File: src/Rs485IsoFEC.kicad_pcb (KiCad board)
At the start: 2 copper layers, 24 x 27.9 mm, 29 parts, among them J1 B3B-XH-A, P1 105444-0001, Q1 DMP3099L-13, U1 FT232RL, U2 ADM2682E

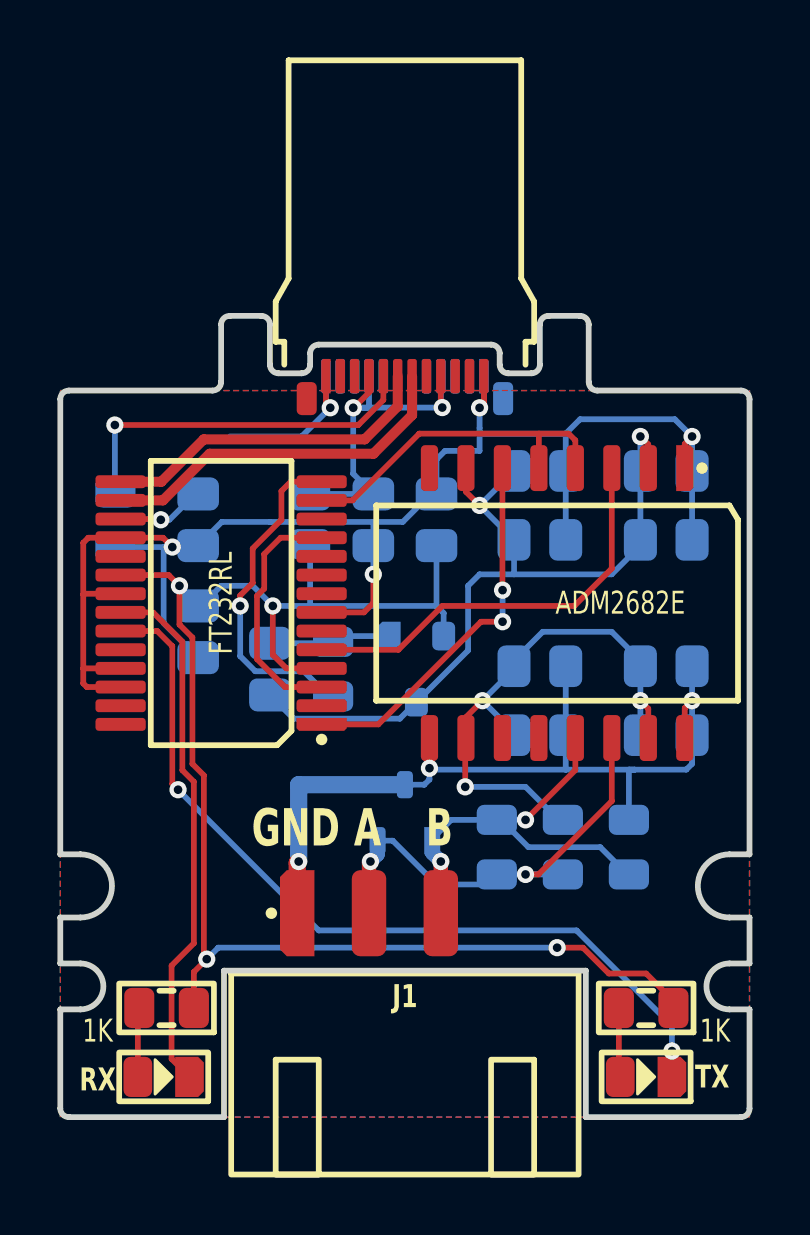
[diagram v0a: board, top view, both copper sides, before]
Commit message: Removed fail-safe termination
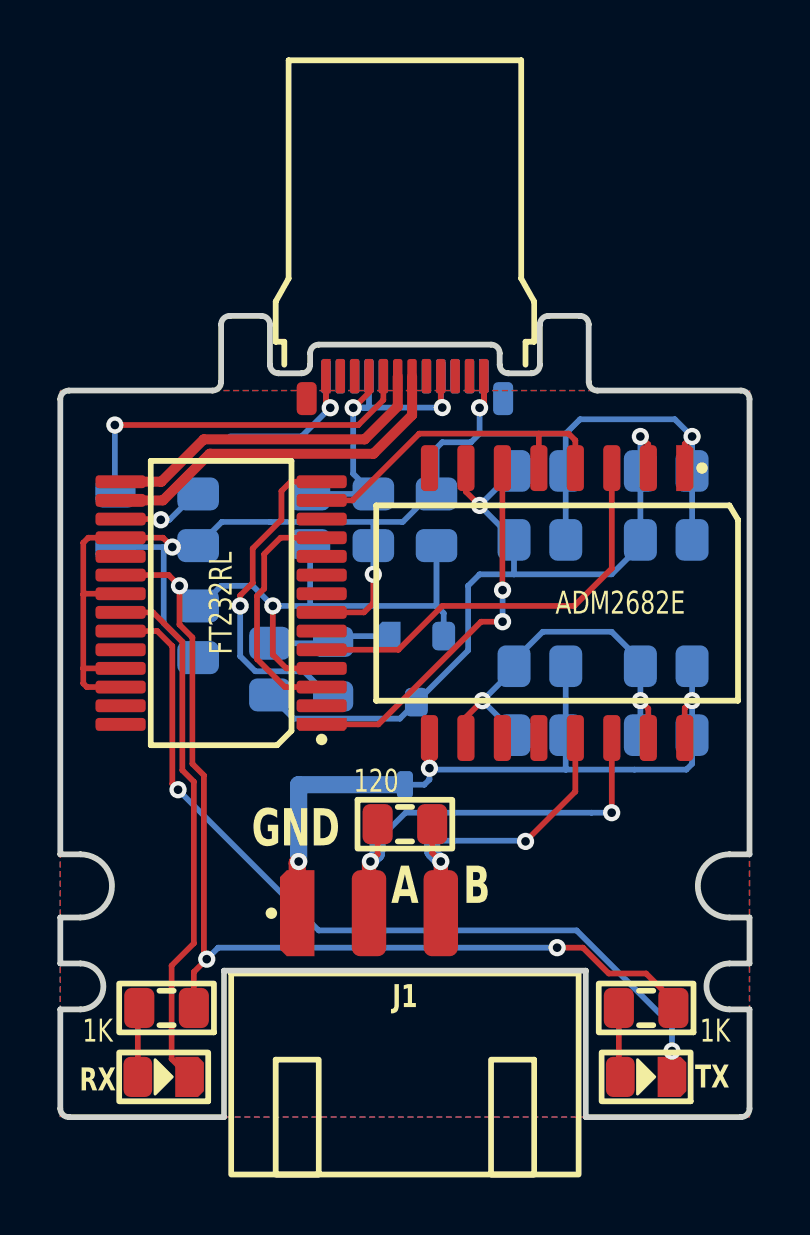
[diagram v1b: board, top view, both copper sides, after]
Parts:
- removed the R2 at (37.5, 38.5)
- removed the R3 at (39.8, 38.5)
- J1: value B3B-XH-A -> B4B-XH-A
- R1: value 130 -> 120; moved to F.Cu
- moved R1 3.30 mm to (32.0, 37.7), turned to 0 degrees
- renumbered R4 to R2, R5 to R3, R6 to R4, R7 to R5
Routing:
- net ISO_V+: track 19.1 -> 13.7 mm, vias 3 -> 2
- net ISO_B: track 14.8 -> 11.6 mm
- net ISO_GND: track 30.2 -> 28.2 mm
- net ISO_A: track 16.2 -> 15.2 mm

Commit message: Refactoring traces a bit + renaming termination resistor
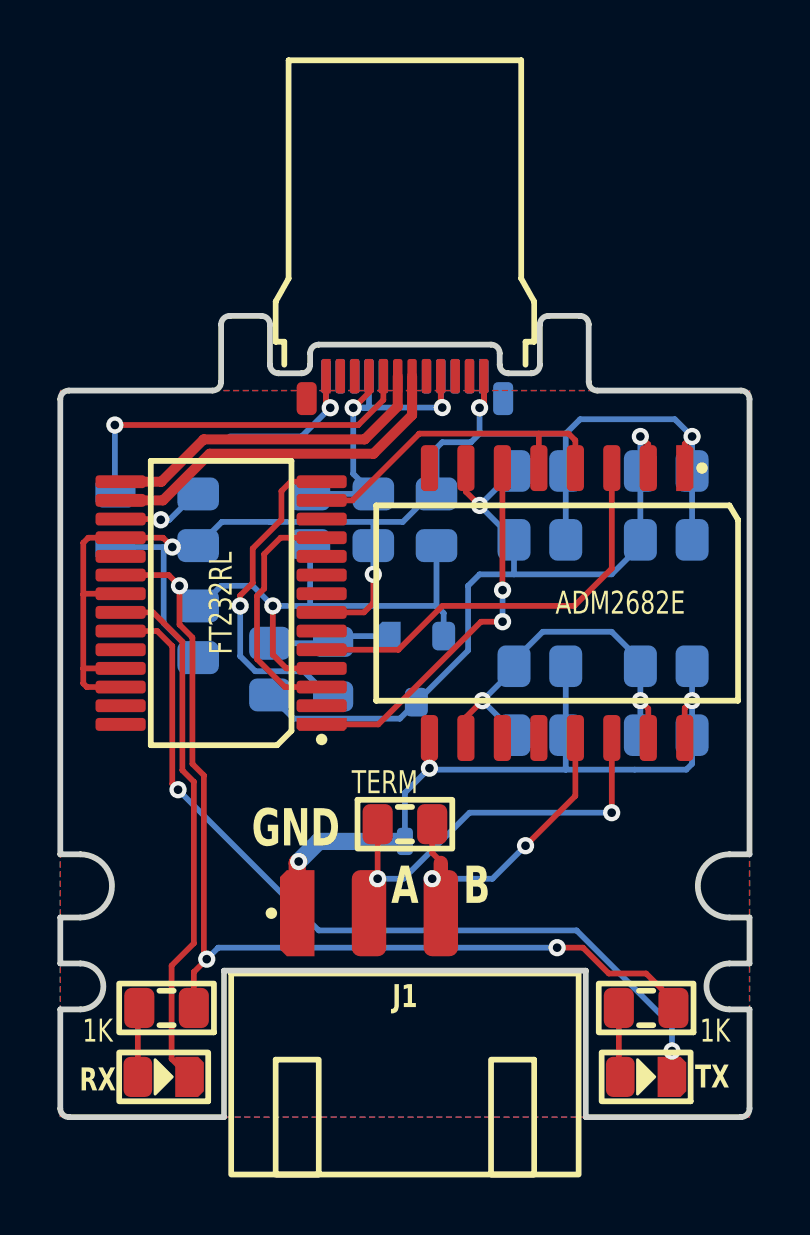
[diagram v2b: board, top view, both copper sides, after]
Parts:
- R1: value 120 -> TERM
- moved D1 1.98 mm to (32.0, 39.3)
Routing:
- net ISO_GND: track 28.2 -> 27.4 mm
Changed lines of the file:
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@@
         (effects (font (size 0.8 0.6) (thickness 0.15)))
     )
-    (fp_text value "120" (at -1 -1.5) (layer "F.SilkS")
+    (fp_text value "TERM" (at -0.7 -1.45) (layer "F.SilkS")
         (effects (font (size 0.8 0.6) (thickness 0.15)))
     )
@@
   )
   (footprint "Medo64:D TVS SM05T1G (SOT23-3)" (layer "B.Cu")
-    (at 32 37.3 180)
+    (at 32 39.275 180)
     (descr "SM05T1G [SM05T1GOSCT-ND]")
     (attr smd)
@@
   (via (at 42 33.4) (size 0.6) (drill 0.3) (layers "F.Cu" "B.Cu") (net 19))
   (via (at 32.855 35.749998) (size 0.6) (drill 0.3) (layers "F.Cu" "B.Cu") (net 19))
-  (segment (start 32 36.325) (end 32.675 36.325) (width 0.2) (layer "B.Cu") (net 19))
   (segment (start 37.6 34.6) (end 37.6 35.8) (width 0.2) (layer "B.Cu") (net 19))
+  (segment (start 28.999998 38.300002) (end 32 38.300002) (width 0.6) (layer "B.Cu") (net 19))
+  (segment (start 32.855 35.749998) (end 32 36.604998) (width 0.2) (layer "B.Cu") (net 19))
+  (segment (start 32 36.604998) (end 32 38.300002) (width 0.2) (layer "B.Cu") (net 19))
+  (segment (start 28.3 39) (end 28.999998 38.300002) (width 0.6) (layer "B.Cu") (net 19))
   (segment (start 32.905002 35.8) (end 32.855 35.749998) (width 0.2) (layer "B.Cu") (net 19))
-  (segment (start 32 36.325) (end 28.3 36.325) (width 0.6) (layer "B.Cu") (net 19))
   (segment (start 41.8 35.8) (end 40 35.8) (width 0.2) (layer "B.Cu") (net 19))
   (segment (start 37.6 32.2) (end 37.6 34.6) (width 0.2) (layer "B.Cu") (net 19))
@@
   (segment (start 40 35.8) (end 37.6 35.8) (width 0.2) (layer "B.Cu") (net 19))
   (segment (start 42 35.6) (end 41.8 35.8) (width 0.2) (layer "B.Cu") (net 19))
-  (segment (start 32.855 36.145) (end 32.855 35.749998) (width 0.2) (layer "B.Cu") (net 19))
   (segment (start 37.6 35.8) (end 32.905002 35.8) (width 0.2) (layer "B.Cu") (net 19))
-  (segment (start 28.3 36.325) (end 28.3 39) (width 0.6) (layer "B.Cu") (net 19))
   (segment (start 42 34.6) (end 42 35.6) (width 0.2) (layer "B.Cu") (net 19))
-  (segment (start 32.675 36.325) (end 32.855 36.145) (width 0.2) (layer "B.Cu") (net 19))
   (segment (start 40.475 34.7) (end 40.475 33.675) (width 0.2) (layer "F.Cu") (net 20))
   (segment (start 34.125 34.7) (end 34.125 33.975) (width 0.2) (layer "F.Cu") (net 20))
@@
   (segment (start 35.8 32.3) (end 34.7 33.4) (width 0.2) (layer "B.Cu") (net 20))
   (segment (start 39.205 37.295) (end 39.2 37.3) (width 0.2) (layer "F.Cu") (net 21))
-  (segment (start 30.75 40.8) (end 30.75 39.05) (width 0.5) (layer "F.Cu") (net 21))
-  (segment (start 31.05 38.75) (end 30.8 39) (width 0.2) (layer "F.Cu") (net 21))
-  (segment (start 30.75 39.05) (end 30.8 39) (width 0.5) (layer "F.Cu") (net 21))
-  (segment (start 31.05 37.7) (end 31.05 38.75) (width 0.2) (layer "F.Cu") (net 21))
+  (segment (start 31.05 37.7) (end 31.05 40.50001) (width 0.2) (layer "F.Cu") (net 21))
   (segment (start 39.205 34.7) (end 39.205 37.295) (width 0.2) (layer "F.Cu") (net 21))
-  (via (at 30.8 39) (size 0.6) (drill 0.3) (layers "F.Cu" "B.Cu") (net 21))
+  (via (at 31.05 39.6) (size 0.6) (drill 0.3) (layers "F.Cu" "B.Cu") (net 21))
   (via (at 39.2 37.3) (size 0.6) (drill 0.3) (layers "F.Cu" "B.Cu") (net 21))
-  (segment (start 38.5 37.3) (end 39.2 37.3) (width 0.2) (layer "B.Cu") (net 21))
-  (segment (start 31.05 38.275) (end 31.05 38.75) (width 0.5) (layer "B.Cu") (net 21))
-  (segment (start 31.05 38.75) (end 30.8 39) (width 0.5) (layer "B.Cu") (net 21))
-  (segment (start 31.05 38.275) (end 32.025 37.3) (width 0.2) (layer "B.Cu") (net 21))
-  (segment (start 32.025 37.3) (end 38.5 37.3) (width 0.2) (layer "B.Cu") (net 21))
-  (segment (start 37.935 34.7) (end 37.935 36.565006) (width 0.2) (layer "F.Cu") (net 22))
+  (segment (start 34.25 37.3) (end 39.2 37.3) (width 0.2) (layer "B.Cu") (net 21))
+  (segment (start 31.05 39.6) (end 31.05 40.50001) (width 0.5) (layer "B.Cu") (net 21))
+  (segment (start 31.05 39.6) (end 31.95 39.6) (width 0.2) (layer "B.Cu") (net 21))
+  (segment (start 31.95 39.6) (end 34.25 37.3) (width 0.2) (layer "B.Cu") (net 21))
   (segment (start 33.25 40.8) (end 33.25 39.05) (width 0.5) (layer "F.Cu") (net 22))
   (segment (start 32.95 37.7) (end 32.95 38.7) (width 0.2) (layer "F.Cu") (net 22))
+  (segment (start 37.935 34.7) (end 37.935 36.715) (width 0.2) (layer "F.Cu") (net 22))
   (segment (start 32.95 38.7) (end 33.25 39) (width 0.2) (layer "F.Cu") (net 22))
-  (segment (start 37.935 36.565006) (end 36.200006 38.3) (width 0.2) (layer "F.Cu") (net 22))
-  (via (at 36.200006 38.3) (size 0.6) (drill 0.3) (layers "F.Cu" "B.Cu") (net 22))
-  (via (at 33.25 39) (size 0.6) (drill 0.3) (layers "F.Cu" "B.Cu") (net 22))
-  (segment (start 32.95 38.275) (end 32.95 38.7) (width 0.5) (layer "B.Cu") (net 22))
-  (segment (start 36.200006 38.3) (end 36.175006 38.275) (width 0.2) (layer "B.Cu") (net 22))
-  (segment (start 32.95 38.7) (end 33.25 39) (width 0.5) (layer "B.Cu") (net 22))
-  (segment (start 36.175006 38.275) (end 32.95 38.275) (width 0.2) (layer "B.Cu") (net 22))
+  (segment (start 37.935 36.715) (end 36.2 38.45) (width 0.2) (layer "F.Cu") (net 22))
+  (via (at 36.2 38.45) (size 0.6) (drill 0.3) (layers "F.Cu" "B.Cu") (net 22))
+  (via (at 32.95 39.6) (size 0.6) (drill 0.3) (layers "F.Cu" "B.Cu") (net 22))
+  (segment (start 36.2 38.45) (end 35.05 39.6) (width 0.2) (layer "B.Cu") (net 22))
+  (segment (start 35.05 39.6) (end 32.95 39.6) (width 0.2) (layer "B.Cu") (net 22))
+  (segment (start 32.95 40.25) (end 32.95 39.6) (width 0.5) (layer "B.Cu") (net 22))
   (zone (net 7) (net_name "GND") (layers "F&B.Cu") (hatch edge 0.5)
     (connect_pads (clearance 0.25))

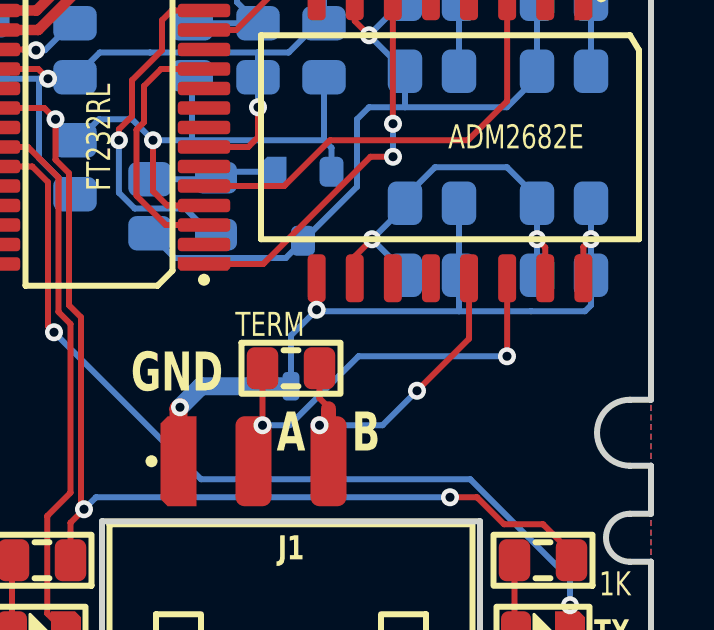
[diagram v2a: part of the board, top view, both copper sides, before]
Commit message: Fixed half-duplex RS-485
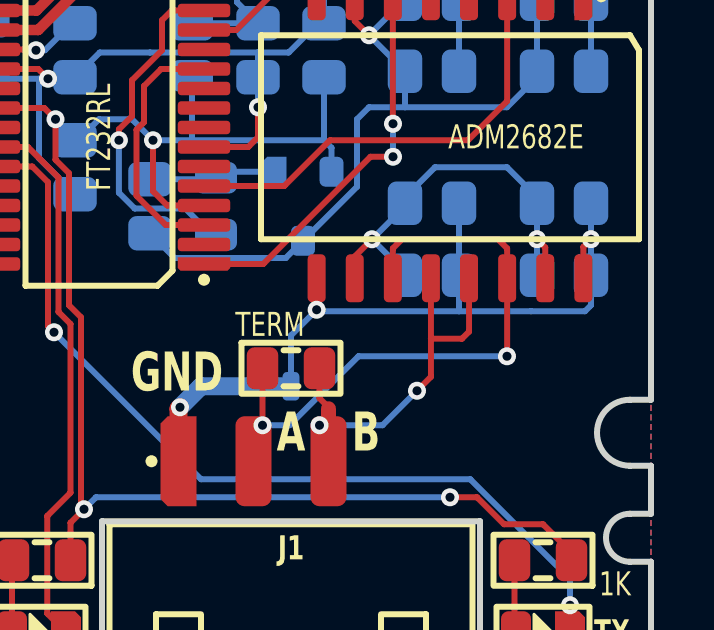
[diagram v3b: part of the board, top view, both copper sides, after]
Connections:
- U2 pad 11: (no net) -> ISO_A
- U2 pad 12: (no net) -> ISO_B
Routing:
- net ISO_A: track 15.4 -> 21.5 mm
- net ISO_B: track 12.0 -> 14.6 mm
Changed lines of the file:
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@@
       (net 20 "ISO_V+") (thermal_bridge_angle 45))
     (pad "11" smd roundrect (at 4.7 1.905 270) (size 1.6 0.6) (layers "F.Cu" "F.Paste" "F.Mask") (roundrect_rratio 0.25)
-      (thermal_bridge_angle 45))
+      (net 21 "ISO_A") (thermal_bridge_angle 45))
     (pad "12" smd roundrect (at 4.7 0.635 270) (size 1.6 0.6) (layers "F.Cu" "F.Paste" "F.Mask") (roundrect_rratio 0.25)
-      (thermal_bridge_angle 45))
+      (net 22 "ISO_B") (thermal_bridge_angle 45))
     (pad "13" smd roundrect (at 4.7 -0.635 270) (size 1.6 0.6) (layers "F.Cu" "F.Paste" "F.Mask") (roundrect_rratio 0.25)
       (net 22 "ISO_B") (thermal_bridge_angle 45))
@@
   (segment (start 35.8 32.3) (end 34.7 33.4) (width 0.2) (layer "B.Cu") (net 20))
   (segment (start 39.205 37.295) (end 39.2 37.3) (width 0.2) (layer "F.Cu") (net 21))
+  (segment (start 39.205 33.705) (end 38.9 33.4) (width 0.2) (layer "F.Cu") (net 21))
+  (segment (start 35.7 33.4) (end 35.395 33.705) (width 0.2) (layer "F.Cu") (net 21))
   (segment (start 31.05 37.7) (end 31.05 40.50001) (width 0.2) (layer "F.Cu") (net 21))
+  (segment (start 39.205 34.7) (end 39.205 33.705) (width 0.2) (layer "F.Cu") (net 21))
+  (segment (start 35.395 33.705) (end 35.395 34.7) (width 0.2) (layer "F.Cu") (net 21))
+  (segment (start 38.9 33.4) (end 35.7 33.4) (width 0.2) (layer "F.Cu") (net 21))
   (segment (start 39.205 34.7) (end 39.205 37.295) (width 0.2) (layer "F.Cu") (net 21))
   (via (at 31.05 39.6) (size 0.6) (drill 0.3) (layers "F.Cu" "B.Cu") (net 21))
@@
   (segment (start 33.25 40.8) (end 33.25 39.05) (width 0.5) (layer "F.Cu") (net 22))
   (segment (start 32.95 37.7) (end 32.95 38.7) (width 0.2) (layer "F.Cu") (net 22))
-  (segment (start 37.935 34.7) (end 37.935 36.715) (width 0.2) (layer "F.Cu") (net 22))
+  (segment (start 37.935 36.48) (end 37.935 34.7) (width 0.2) (layer "F.Cu") (net 22))
+  (segment (start 36.665 37.985) (end 36.2 38.45) (width 0.2) (layer "F.Cu") (net 22))
   (segment (start 32.95 38.7) (end 33.25 39) (width 0.2) (layer "F.Cu") (net 22))
-  (segment (start 37.935 36.715) (end 36.2 38.45) (width 0.2) (layer "F.Cu") (net 22))
+  (segment (start 36.665 34.7) (end 36.665 36.715) (width 0.2) (layer "F.Cu") (net 22))
+  (segment (start 37.7 36.715) (end 37.935 36.48) (width 0.2) (layer "F.Cu") (net 22))
+  (segment (start 36.665 36.715) (end 37.7 36.715) (width 0.2) (layer "F.Cu") (net 22))
+  (segment (start 36.665 36.715) (end 36.665 37.985) (width 0.2) (layer "F.Cu") (net 22))
   (via (at 36.2 38.45) (size 0.6) (drill 0.3) (layers "F.Cu" "B.Cu") (net 22))
   (via (at 32.95 39.6) (size 0.6) (drill 0.3) (layers "F.Cu" "B.Cu") (net 22))

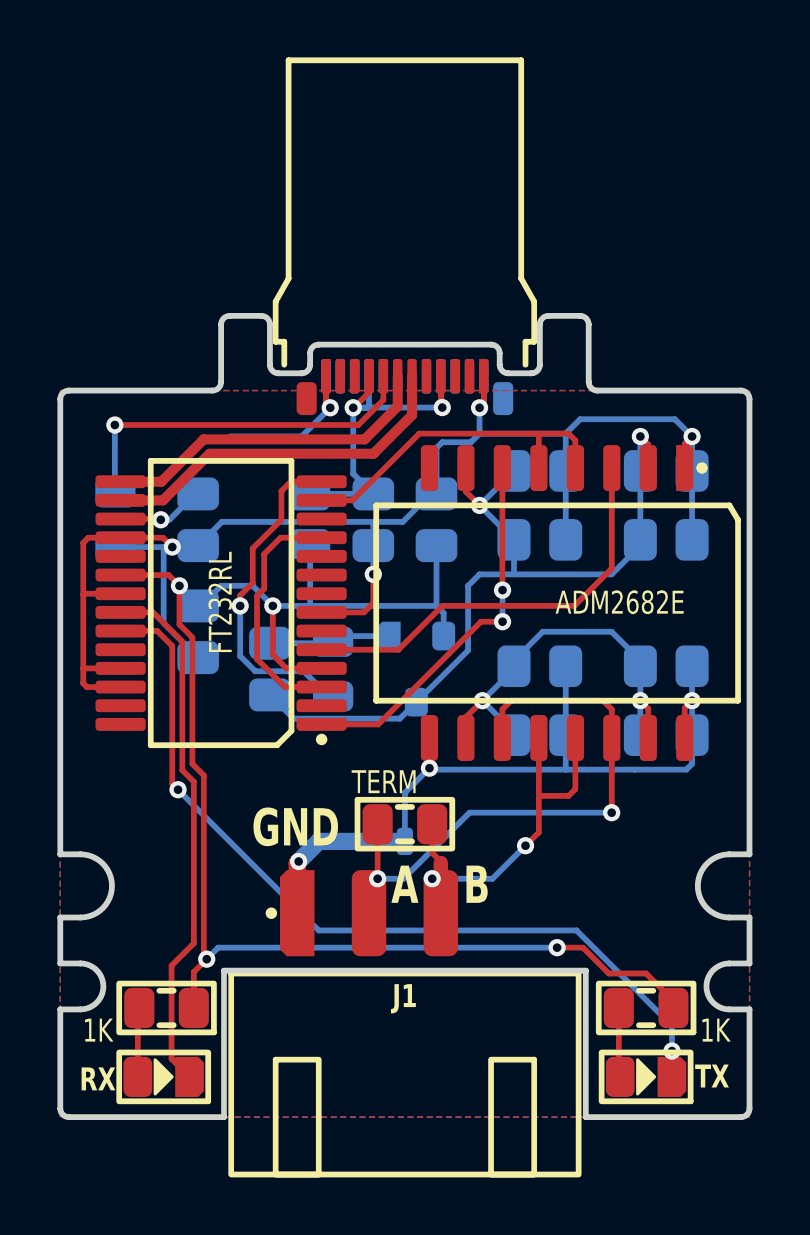
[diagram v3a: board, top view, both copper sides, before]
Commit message: Refactoring isolator orientation
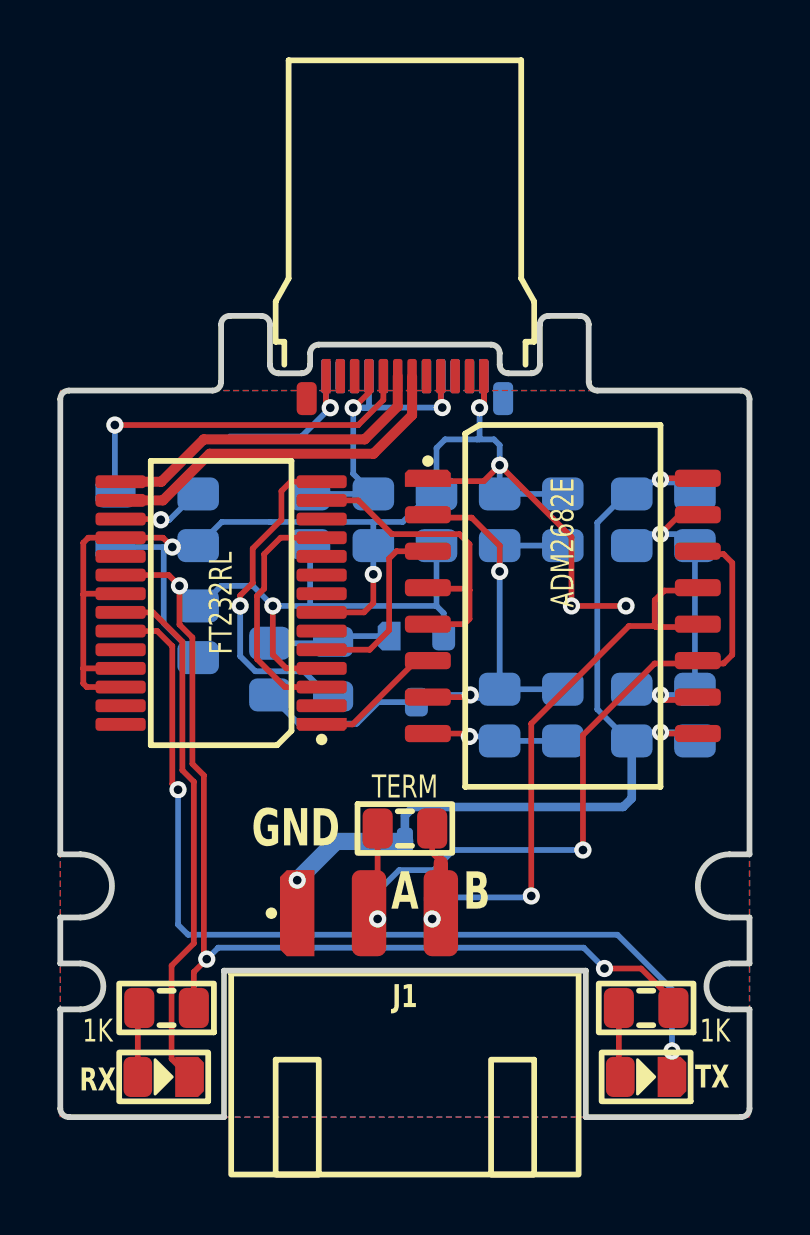
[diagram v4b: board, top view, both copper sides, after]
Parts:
- moved C9 8.61 mm to (35.3, 33.9), turned to 90 degrees
- moved C3 7.57 mm to (42.1, 27.1), turned to -90 degrees
- moved C12 6.15 mm to (37.5, 33.9), turned to 90 degrees
- moved C2 6.04 mm to (35.3, 27.1), turned to -90 degrees
- moved C10 5.45 mm to (42.1, 33.9), turned to 90 degrees
- moved C8 5.24 mm to (39.9, 27.1), turned to -90 degrees
- moved C7 3.67 mm to (37.5, 27.1), turned to -90 degrees
- moved C13 3.62 mm to (39.9, 33.9), turned to 90 degrees
- moved U2 0.22 mm to (37.5, 30.1), turned to 0 degrees
- moved R1 0.15 mm to (32.0, 37.9)
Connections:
- U2 pad 8: (no net) -> GND
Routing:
- net ISO_B: track 14.6 -> 24.3 mm
- net TXD: track 13.1 -> 4.07 mm, vias 2 -> 0
- net RXD: track 14.8 -> 6.59 mm
- net ISO_A: track 21.5 -> 26.8 mm
- net ISO_GND: track 27.4 -> 32.0 mm
- net LED_TXD: track 29.5 -> 33.0 mm
- net 5V_SW: track 28.0 -> 24.5 mm
- net GND: track 64.2 -> 67.7 mm, vias 5 -> 8
- net ISO_V+: track 13.7 -> 10.8 mm
- net TXDEN: track 12.1 -> 11.3 mm

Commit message: Moving LEDs to bottom
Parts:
- DS1, DS2, R2, R3: moved to B.Cu
- moved R2 0.10 mm to (23.6, 44.1), turned to 0 degrees
- turned DS1 to 0 degrees
- turned DS2 to 0 degrees
- turned R3 to 0 degrees
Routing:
- net LED_RXD: track 18.5 -> 19.8 mm, vias 0 -> 1
- net LED_TXD: track 33.0 -> 32.7 mm, vias 2 -> 1
- net 5V: track 53.4 -> 53.5 mm, vias 4 -> 3
